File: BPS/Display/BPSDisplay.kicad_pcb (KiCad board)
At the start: 2 copper layers, 65 x 56 mm, 5 parts, among them P1 Conn_02x20_Odd_Even

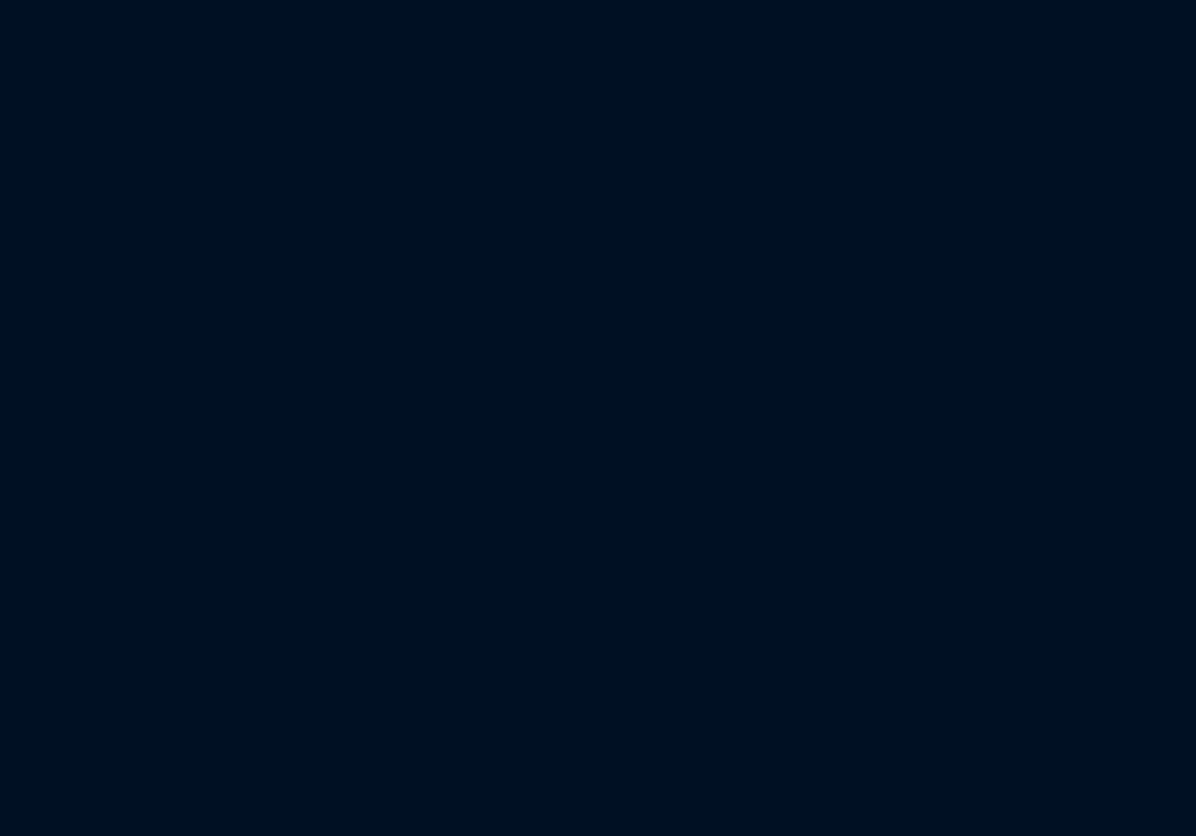
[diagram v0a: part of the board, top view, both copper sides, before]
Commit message: Creates schematics for display.
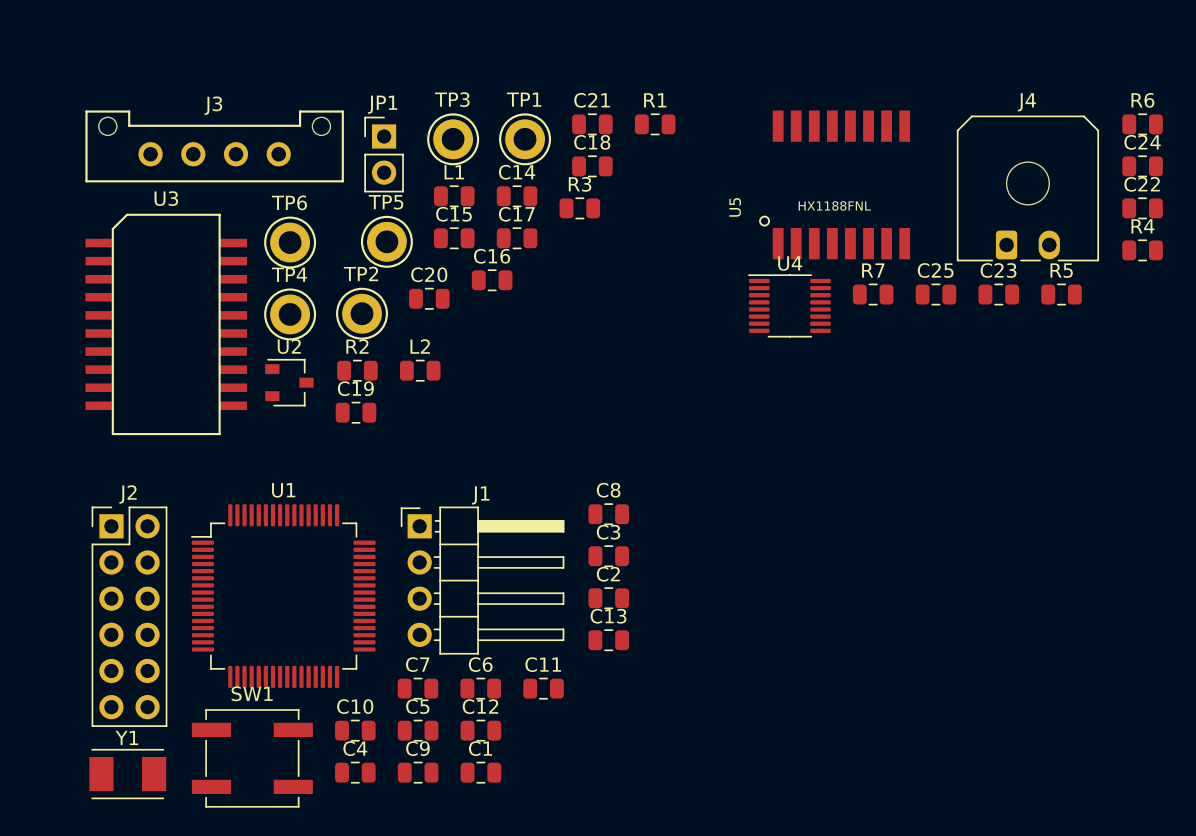
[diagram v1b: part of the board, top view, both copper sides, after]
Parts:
- added C1: 0.1u, Capacitor_SMD:C_0805_2012Metric, F.Cu at (366.1, 154.1)
- added C10: 0.1u, Capacitor_SMD:C_0805_2012Metric, F.Cu at (357.3, 151.1)
- added C11: 2.2u, Capacitor_SMD:C_0805_2012Metric, F.Cu at (370.5, 148.2)
- added C12: 8p, Capacitor_SMD:C_0805_2012Metric, F.Cu at (366.1, 151.1)
- added C13: 8p, Capacitor_SMD:C_0805_2012Metric, F.Cu at (375.1, 144.8)
- added C14: 0.22uF, Capacitor_SMD:C_0805_2012Metric, F.Cu at (368.7, 113.6)
- added C15: 10uF, Capacitor_SMD:C_0805_2012Metric, F.Cu at (364.3, 116.6)
- added C16: 0.1uF, Capacitor_SMD:C_0805_2012Metric, F.Cu at (366.9, 119.5)
- added C17: 0.01uF, Capacitor_SMD:C_0805_2012Metric, F.Cu at (368.7, 116.6)
- added C18: 10uF, Capacitor_SMD:C_0805_2012Metric, F.Cu at (374.0, 111.5)
- added C19: 0.1uF, Capacitor_SMD:C_0805_2012Metric, F.Cu at (357.4, 128.8)
- added C2: 0.1u, Capacitor_SMD:C_0805_2012Metric, F.Cu at (375.1, 141.8)
- added C20: 0.1uF, Capacitor_SMD:C_0805_2012Metric, F.Cu at (362.5, 120.8)
- added C21: 0.01uF, Capacitor_SMD:C_0805_2012Metric, F.Cu at (374.0, 108.6)
- added C22: 0.01u, Capacitor_SMD:C_0805_2012Metric, F.Cu at (412.6, 114.5)
- added C23: 0.01u, Capacitor_SMD:C_0805_2012Metric, F.Cu at (402.5, 120.5)
- added C24: 0.1u, Capacitor_SMD:C_0805_2012Metric, F.Cu at (412.6, 111.5)
- added C25: 0.1u, Capacitor_SMD:C_0805_2012Metric, F.Cu at (398.1, 120.5)
- added C3: 0.1u, Capacitor_SMD:C_0805_2012Metric, F.Cu at (375.1, 138.9)
- added C4: 0.1u, Capacitor_SMD:C_0805_2012Metric, F.Cu at (357.3, 154.1)
- added C5: 0.1u, Capacitor_SMD:C_0805_2012Metric, F.Cu at (361.7, 151.1)
- added C6: 0.1u, Capacitor_SMD:C_0805_2012Metric, F.Cu at (366.1, 148.2)
- added C7: 4.7u, Capacitor_SMD:C_0805_2012Metric, F.Cu at (361.7, 148.2)
- added C8: 0.1u, Capacitor_SMD:C_0805_2012Metric, F.Cu at (375.1, 135.9)
- added C9: 1u, Capacitor_SMD:C_0805_2012Metric, F.Cu at (361.7, 154.1)
- added J1: SWD, Connector_PinHeader_2.54mm:PinHeader_1x04_P2.54mm_Horizontal, F.Cu at (361.8, 136.8)
- added J2: Conn_02x06_Counter_Clockwise, Connector_PinHeader_2.54mm:PinHeader_2x06_P2.54mm_Vertical, F.Cu at (340.2, 136.8)
- added J3: CAN_Out, UTSVT_Connectors:Molex_MicroFit3.0_1x4xP3.00mm_PolarizingPeg_Vertical, F.Cu at (342.9, 110.7)
- added J4: isoSPI_Display, Connector_Molex:Molex_Micro-Fit_3.0_43650-0200_1x02_P3.00mm_Horizontal, F.Cu at (403.0, 117.0)
- added JP1: Termination Resistors, Connector_PinHeader_2.54mm:PinHeader_1x02_P2.54mm_Vertical, F.Cu at (359.3, 109.4)
- added L1: 2kH, Inductor_SMD:L_0805_2012Metric, F.Cu at (364.3, 113.6)
- added L2: 2kH, Inductor_SMD:L_0805_2012Metric, F.Cu at (361.9, 125.9)
- added R1: 60, Resistor_SMD:R_0805_2012Metric, F.Cu at (378.4, 108.6)
- added R2: 60, Resistor_SMD:R_0805_2012Metric, F.Cu at (357.5, 125.9)
- added R3: 0, Resistor_SMD:R_0805_2012Metric, F.Cu at (373.1, 114.5)
- added R4: 49.9, Resistor_SMD:R_0805_2012Metric, F.Cu at (412.6, 117.4)
- added R5: 806, Resistor_SMD:R_0805_2012Metric, F.Cu at (406.9, 120.5)
- added R6: 1.21k, Resistor_SMD:R_0805_2012Metric, F.Cu at (412.6, 108.6)
- added R7: 49.9, Resistor_SMD:R_0805_2012Metric, F.Cu at (393.7, 120.5)
- added SW1: Reset, Button_Switch_SMD:SW_SPST_B3SL-1002P, F.Cu at (350.1, 153.1)
- added TP1: CAN_ISO_Vout, TestPoint:TestPoint_Keystone_5005-5009_Compact, F.Cu at (369.2, 109.6)
- added TP2: CAN_ISO_Vin, TestPoint:TestPoint_Keystone_5005-5009_Compact, F.Cu at (357.8, 121.9)
- added TP3: CAN_ISO_GndIn, TestPoint:TestPoint_Keystone_5005-5009_Compact, F.Cu at (364.2, 109.6)
- added TP4: CAN_ISO_GndOut, TestPoint:TestPoint_Keystone_5005-5009_Compact, F.Cu at (352.7, 121.9)
- added TP5: CAN_H, TestPoint:TestPoint_Keystone_5005-5009_Compact, F.Cu at (359.5, 116.8)
- added TP6: CAN_L, TestPoint:TestPoint_Keystone_5005-5009_Compact, F.Cu at (352.7, 116.9)
- added U1: STM32F413RHTx, Package_QFP:LQFP-64_10x10mm_P0.5mm, F.Cu at (352.3, 141.7)
- added U2: CDSOT23-T24CAN, Package_TO_SOT_SMD:SOT-23W, F.Cu at (352.7, 126.7)
- added U3: ADM3055E, UTSVT_ICs:SOIC-20W_7.5x15.4mm_Pitch1.27mm, F.Cu at (344.0, 122.6)
- added U4: LTC6820, Package_SO:MSOP-16_3x4mm_P0.5mm, F.Cu at (387.8, 121.3)
- added U5: HX1188FNL, UTSVT_BPS:HXXXX, F.Cu at (391.4, 112.8)
- added Y1: 8M, Crystal:Crystal_SMD_TXC_7A-2Pin_5x3.2mm, F.Cu at (341.3, 154.2)
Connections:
- P1 pad 33: /GPIO13(PWM1) -> /GPIO13
- P1 pad 35: /GPIO19(SPI1_MISO) -> /GPIO19

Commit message: Display, Board Layout
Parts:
- removed TP1: CAN_ISO_Vout, TestPoint:TestPoint_Keystone_5005-5009_Compact
- removed TP2: CAN_ISO_Vin, TestPoint:TestPoint_Keystone_5005-5009_Compact
- removed TP3: CAN_ISO_GndIn, TestPoint:TestPoint_Keystone_5005-5009_Compact
- removed TP4: CAN_ISO_GndOut, TestPoint:TestPoint_Keystone_5005-5009_Compact
- removed TP5: CAN_H, TestPoint:TestPoint_Keystone_5005-5009_Compact
- removed TP6: CAN_L, TestPoint:TestPoint_Keystone_5005-5009_Compact
- C15, C17, C24, C25, J2, R2, U2, U5: moved to B.Cu
- J3: footprint UTSVT_Connectors:Molex_MicroFit3.0_1x4xP3.00mm_PolarizingPeg_Vertical -> Connector_Molex:Molex_Micro-Fit_3.0_43650-0400_1x04_P3.00mm_Horizontal
- moved J4 195.0 mm to (209.4, 140.1), turned to 90 degrees
- moved R4 188.8 mm to (224.9, 137.3)
- moved R6 186.1 mm to (230.2, 145.4)
- moved C22 184.0 mm to (230.1, 138.6)
- moved R5 178.8 mm to (230.2, 147.6)
- moved C24 177.0 mm to (238.1, 141.6)
- moved U5 176.1 mm to (217.8, 141.7), turned to 270 degrees
- moved C23 173.0 mm to (230.1, 136.0)
- moved R7 169.9 mm to (224.9, 139.8)
- moved R1 167.0 mm to (212.0, 123.1), turned to 270 degrees
- moved C25 164.2 mm to (236.2, 148.5), turned to 180 degrees
- moved C17 154.3 mm to (214.8, 128.5), turned to 90 degrees
- moved C16 153.8 mm to (213.4, 128.5), turned to 90 degrees
- moved R3 153.2 mm to (220.0, 119.5), turned to 90 degrees
- moved C15 152.7 mm to (212.0, 128.5), turned to 90 degrees
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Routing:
- net +3V3: track 0.00 -> 88.1 mm, vias 0 -> 7
- net Net-(C15-Pad2): track 0.00 -> 39.1 mm
- net /NRST: track 0.00 -> 36.5 mm
- net /isoSPI/DISP_IP: track 0.00 -> 28.1 mm, vias 0 -> 3
- net /CAN2_TX: track 0.00 -> 24.2 mm, vias 0 -> 2
- net Net-(C15-Pad1): track 0.00 -> 22.6 mm
- net /CAN2_RX: track 0.00 -> 22.1 mm, vias 0 -> 2
- net /isoSPI/DISP_IM: track 0.00 -> 21.0 mm, vias 0 -> 1
- net /CAN/CAN_H: track 0.00 -> 19.8 mm
- net /SWDIO: track 0.00 -> 17.9 mm, vias 0 -> 1
- net /CAN/CAN_L: track 0.00 -> 14.0 mm, vias 0 -> 1
- net Net-(C13-Pad1): track 0.00 -> 13.6 mm
- net Net-(C23-Pad1): track 0.00 -> 13.0 mm
- net Net-(C22-Pad1): track 0.00 -> 12.5 mm, vias 0 -> 1
- net Net-(J4-Pad2): track 0.00 -> 11.6 mm
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- added copper zone on B.Cu, net GND
- added copper zone on F.Cu, net GND

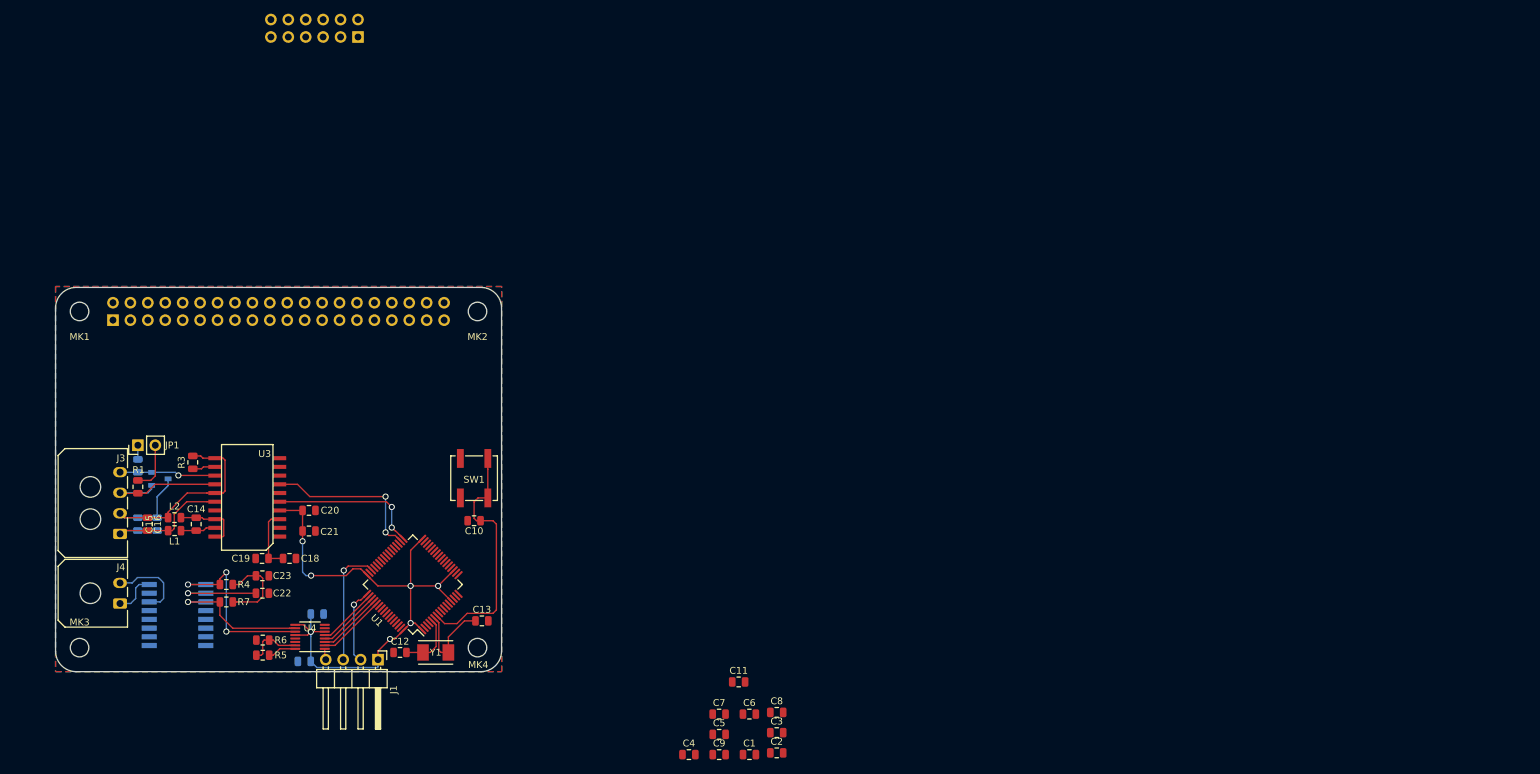
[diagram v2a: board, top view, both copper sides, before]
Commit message: Adds display board
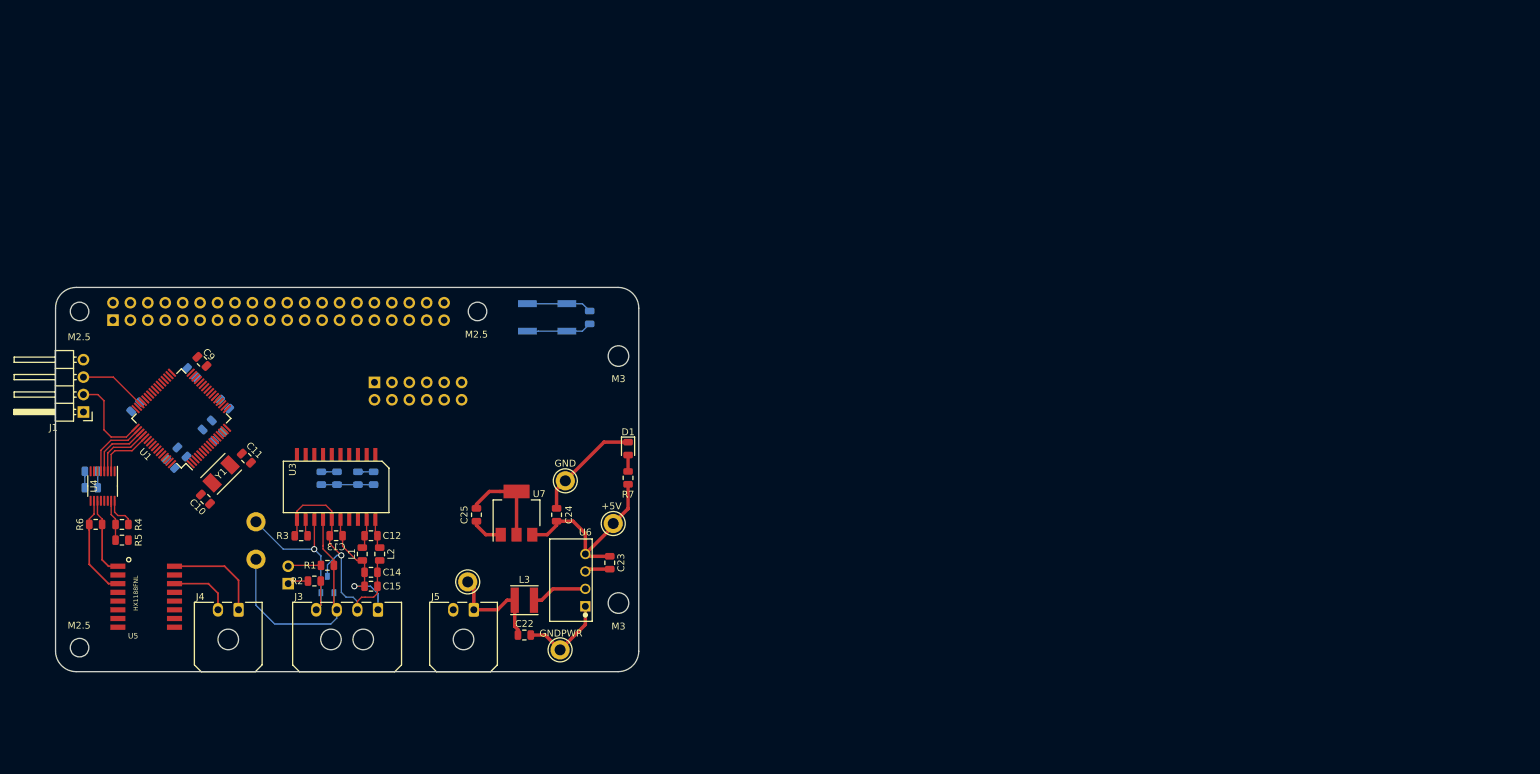
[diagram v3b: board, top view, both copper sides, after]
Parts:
- removed the C8 at (305.1, 155.9)
- removed the MK4 at (261.5, 146.5)
- added C10: 8p, Capacitor_SMD:C_0805_2012Metric, F.Cu at (221.8, 124.9)
- added D1: PowerOn, LED_SMD:LED_0805_2012Metric, F.Cu at (283.4, 117.5)
- added J5: CarPowerConnector, Connector_Molex:Molex_Micro-Fit_3.0_43650-0200_1x02_P3.00mm_Horizontal, F.Cu at (261.0, 141.0)
- added L3: 6.8u, Inductor_SMD:L_Taiyo-Yuden_MD-4040, F.Cu at (268.3, 139.6)
- added MK3: M3, MountingHole:MountingHole_3mm, F.Cu at (282.0, 104.0)
- added MK5: M3, MountingHole:MountingHole_3mm, F.Cu at (282.0, 140.0)
- added TP1: CAN_H, TestPoint:TestPoint_Keystone_5005-5009_Compact, B.Cu at (229.2, 133.6)
- added TP2: CAN_L, TestPoint:TestPoint_Keystone_5005-5009_Compact, B.Cu at (229.2, 128.2)
- added TP3: +3.3V_TP, TestPoint:TestPoint_Keystone_5005-5009_Compact, F.Cu at (281.3, 128.4)
- added TP4: +12V_TP, TestPoint:TestPoint_Keystone_5005-5009_Compact, F.Cu at (260.1, 136.9)
- added TP5: GNDPWR_TP, TestPoint:TestPoint_Keystone_5005-5009_Compact, F.Cu at (273.5, 146.8)
- added TP6: GND_TP, TestPoint:TestPoint_Keystone_5005-5009_Compact, F.Cu at (274.3, 122.2)
- added U6: PDS1-S12-S5, UTSVT_ICs:PDSx-S, F.Cu at (277.2, 136.7)
- added U7: NCP1117-3.3_SOT223, Package_TO_SOT_SMD:SOT-223-3_TabPin2, F.Cu at (267.2, 126.9)
- C1, C2, C3, C4, C6, JP1, SW1: moved to B.Cu
- C11: value 2.2u -> 8p
- C12: value 8p -> 0.22uF
- C13: value 8p -> 10uF
- C14: value 0.22uF -> 0.1uF
- C15: value 10uF -> 0.01uF; moved to F.Cu
- C16: value 0.1uF -> 10uF; moved to B.Cu
- C17: value 0.01uF -> 0.1uF
- C18: value 10uF -> 0.1uF; moved to B.Cu
- C19: value 0.1uF -> 0.01uF; moved to B.Cu
- C20: value 0.1uF -> 0.1u; moved to B.Cu
- C21: value 0.01uF -> 0.1u; moved to B.Cu
- C22, C23: value 0.01u -> 4.7u
- C24, C25: value 0.1u -> 10u; moved to F.Cu
- C5: value 0.1u -> 4.7u; moved to B.Cu
- C7: value 4.7u -> 1u; moved to B.Cu
- C8: renamed from C10; moved to B.Cu
- C9: value 1u -> 2.2u
- R2, U5: moved to F.Cu
- R4: value 49.9 -> 806
- R5: value 806 -> 1.21k
- R6: value 1.21k -> 120
- R7: value 49.9 -> 1.5k
- moved C3 100.1 mm to (219.8, 106.4), turned to 315 degrees
- moved C2 97.9 mm to (216.8, 119.6), turned to 135 degrees
- moved C4 95.2 mm to (211.7, 111.4), turned to 45 degrees
- moved C9 94.7 mm to (221.3, 104.8), turned to 135 degrees
- moved C1 92.0 mm to (224.6, 111.0), turned to 315 degrees
- moved C5 88.5 mm to (218.4, 118.0), turned to 135 degrees
- moved C6 87.3 mm to (223.7, 115.7), turned to 225 degrees
- moved C7 85.7 mm to (222.1, 114.1), turned to 225 degrees
- moved C11 78.8 mm to (227.8, 118.9), turned to 315 degrees
- moved R7 61.3 mm to (283.4, 121.8), turned to 90 degrees
- moved J1 56.1 mm to (204.1, 112.2), turned to 180 degrees
- moved C23 50.7 mm to (280.8, 134.1), turned to 270 degrees
- moved J2 50.4 mm to (246.5, 107.8), turned to 270 degrees
- moved U1 41.5 mm to (218.3, 113.1)
- moved Y1 40.7 mm to (224.1, 121.2), turned to 45 degrees
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- renumbered MK3 to MK2, MK2 to MK4
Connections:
- C12 pad 2: GND -> Net-(C12-Pad2)
- C13 pad 2: GND -> Net-(C13-Pad2)
- C14 pad 1: Net-(C14-Pad1) -> Net-(C13-Pad1)
- C14 pad 2: Net-(C14-Pad2) -> Net-(C13-Pad2)
- C15 pad 1: Net-(C15-Pad1) -> Net-(C13-Pad1)
- C15 pad 2: Net-(C15-Pad2) -> Net-(C13-Pad2)
- C16 pad 1: Net-(C15-Pad1) -> +5V
- C16 pad 2: Net-(C15-Pad2) -> GND
- C17 pad 1: Net-(C15-Pad1) -> +5V
- C17 pad 2: Net-(C15-Pad2) -> GND
- C18 pad 1: +5V -> +3V3
- C19 pad 1: +5V -> +3V3
- C22 pad 1: Net-(C22-Pad1) -> +12V
- C22 pad 2: GND -> GNDPWR
- C23 pad 1: Net-(C23-Pad1) -> +5V
- C24 pad 1: +3V3 -> +5V
- C9 pad 1: +3V3 -> Net-(C9-Pad1)
- J3 pad 1: Net-(C15-Pad1) -> Net-(C13-Pad1)
- J3 pad 2: Net-(C15-Pad2) -> Net-(C13-Pad2)
- L1 pad 1: Net-(C15-Pad1) -> Net-(C13-Pad1)
- L1 pad 2: Net-(C14-Pad1) -> Net-(C12-Pad1)
- L2 pad 1: Net-(C15-Pad2) -> Net-(C13-Pad2)
- L2 pad 2: Net-(C14-Pad2) -> Net-(C12-Pad2)
- P1 pad 10: /GPIO15(RXD0) -> (no net)
- P1 pad 12: /GPIO18(GEN1)(PWM0) -> (no net)
- P1 pad 13: /GPIO27(GEN2) -> (no net)
- P1 pad 15: /GPIO22(GEN3) -> (no net)
- P1 pad 16: /GPIO23(GEN4) -> (no net)
- P1 pad 26: /GPIO7(SPI1_CE_N) -> (no net)
- P1 pad 27: /ID_SD -> (no net)
- P1 pad 28: /ID_SC -> (no net)
- P1 pad 3: /GPIO2(SDA1) -> (no net)
- P1 pad 32: /GPIO12(PWM0) -> (no net)
- P1 pad 36: /GPIO16 -> (no net)
- P1 pad 37: /GPIO26 -> (no net)
- P1 pad 38: /GPIO20(SPI1_MOSI) -> (no net)
- P1 pad 40: /GPIO21(SPI1_SCK) -> (no net)
- P1 pad 5: /GPIO3(SCL1) -> (no net)
- P1 pad 7: /GPIO4(GCLK) -> (no net)
- P1 pad 8: /GPIO14(TXD0) -> (no net)
- R3 pad 2: Net-(C15-Pad2) -> Net-(C13-Pad2)
- R4 pad 1: /isoSPI/DISP_IP -> Net-(R4-Pad1)
- R4 pad 2: Net-(C23-Pad1) -> Net-(R4-Pad2)
- R5 pad 1: Net-(R5-Pad1) -> GND
- R5 pad 2: Net-(R5-Pad2) -> Net-(R4-Pad1)
- R6 pad 1: GND -> /isoSPI/DISP_IM
- R6 pad 2: Net-(R5-Pad1) -> /isoSPI/DISP_IP
- R7 pad 1: /isoSPI/DISP_IM -> +5V
- R7 pad 2: Net-(C23-Pad1) -> Net-(D1-Pad2)
- U1 pad 10: Net-(U1-Pad10) -> (no net)
- U1 pad 11: Net-(U1-Pad11) -> (no net)
- U1 pad 14: Net-(U1-Pad14) -> (no net)
- U1 pad 15: Net-(U1-Pad15) -> (no net)
- U1 pad 16: Net-(U1-Pad16) -> (no net)
- U1 pad 17: Net-(U1-Pad17) -> (no net)
- U1 pad 2: Net-(U1-Pad2) -> (no net)
- U1 pad 20: Net-(U1-Pad20) -> (no net)
- U1 pad 24: Net-(U1-Pad24) -> (no net)
- U1 pad 25: Net-(U1-Pad25) -> (no net)
- U1 pad 29: Net-(U1-Pad29) -> (no net)
- U1 pad 3: Net-(U1-Pad3) -> (no net)
- U1 pad 30: Net-(C11-Pad1) -> Net-(C9-Pad1)
- U1 pad 35: Net-(U1-Pad35) -> (no net)
- U1 pad 36: Net-(U1-Pad36) -> (no net)
- U1 pad 39: Net-(U1-Pad39) -> (no net)
- U1 pad 4: Net-(U1-Pad4) -> (no net)
- U1 pad 40: Net-(U1-Pad40) -> (no net)
- U1 pad 45: Net-(U1-Pad45) -> (no net)
- U1 pad 5: Net-(C12-Pad1) -> Net-(C10-Pad1)
- U1 pad 54: Net-(U1-Pad54) -> (no net)
- U1 pad 56: Net-(U1-Pad56) -> (no net)
- U1 pad 57: Net-(U1-Pad57) -> (no net)
- U1 pad 58: Net-(U1-Pad58) -> (no net)
- U1 pad 59: Net-(U1-Pad59) -> (no net)
- U1 pad 6: Net-(C13-Pad1) -> Net-(C11-Pad1)
- U1 pad 60: Net-(U1-Pad60) -> GND
- U1 pad 61: Net-(U1-Pad61) -> (no net)
- U1 pad 62: Net-(U1-Pad62) -> (no net)
- U1 pad 8: Net-(U1-Pad8) -> (no net)
- U1 pad 9: Net-(U1-Pad9) -> (no net)
- U2 pad 3: Net-(C15-Pad2) -> Net-(C13-Pad2)
- U3 pad 11: Net-(C15-Pad2) -> Net-(C13-Pad2)
- U3 pad 15: Net-(C15-Pad2) -> Net-(C13-Pad2)
- U3 pad 16: Net-(C15-Pad1) -> Net-(C13-Pad1)
- U3 pad 17: Net-(U3-Pad17) -> (no net)
- U3 pad 18: Net-(C14-Pad2) -> Net-(C12-Pad2)
- U3 pad 19: Net-(C14-Pad1) -> Net-(C12-Pad1)
- U3 pad 20: Net-(C14-Pad2) -> Net-(C12-Pad2)
- U3 pad 6: Net-(U3-Pad6) -> (no net)
- U3 pad 8: Net-(U3-Pad8) -> (no net)
- U3 pad 9: Net-(U3-Pad9) -> (no net)
- U4 pad 15: Net-(R5-Pad1) -> Net-(R4-Pad1)
- U4 pad 16: Net-(R5-Pad2) -> Net-(R4-Pad2)
- U5 pad 10: Net-(U5-Pad10) -> (no net)
- U5 pad 11: Net-(U5-Pad11) -> (no net)
- U5 pad 15: Net-(U5-Pad15) -> (no net)
- U5 pad 2: Net-(C22-Pad1) -> (no net)
- U5 pad 6: Net-(U5-Pad6) -> (no net)
- U5 pad 7: Net-(U5-Pad7) -> (no net)
- U5 pad 8: Net-(U5-Pad8) -> (no net)
- U5 pad 9: Net-(U5-Pad9) -> (no net)
- Y1 pad 1: Net-(C12-Pad1) -> Net-(C10-Pad1)
- Y1 pad 2: Net-(C13-Pad1) -> Net-(C11-Pad1)
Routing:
- net +3V3: track 88.1 -> 18.2 mm, vias 7 -> 0
- net GND: track 1.64 -> 44.0 mm
- net Net-(C13-Pad2): track 0.00 -> 40.1 mm, vias 0 -> 1
- net Net-(C15-Pad2): track 39.1 -> 0.00 mm
- net /NRST: track 36.5 -> 9.52 mm
- net /CAN2_TX: track 24.2 -> 0.00 mm, vias 2 -> 0
- net Net-(C15-Pad1): track 22.6 -> 0.00 mm
- net +5V: track 9.23 -> 31.3 mm
- net /CAN2_RX: track 22.1 -> 0.00 mm, vias 2 -> 0
- net /CAN/CAN_H: track 19.8 -> 37.9 mm
- net /isoSPI/DISP_IP: track 28.1 -> 11.6 mm, vias 3 -> 0
- net +12V: track 0.00 -> 16.2 mm
- net /CAN/CAN_L: track 14.0 -> 28.5 mm
- net GNDPWR: track 0.00 -> 13.0 mm
- net Net-(C23-Pad1): track 13.0 -> 0.00 mm
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- removed copper zone on B.Cu, net GND
- removed copper zone on F.Cu, net GND
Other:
- board size 65 x 56 mm -> 85 x 56 mm
- board text added: "+12V"
- board text added: "+5V"
- board text added: "GND"
- board text added: "GNDPWR"
- board text added: "M2.5"
- board text added: "M3"
